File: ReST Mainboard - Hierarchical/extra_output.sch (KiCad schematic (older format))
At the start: 16 parts, among them P28 CONN_02X02, P32 CONN_02X02, P33 CONN_02X02, P34 CONN_02X02, Q1 TBD, Q2 TBD, Q3 TBD, Q4 TBD

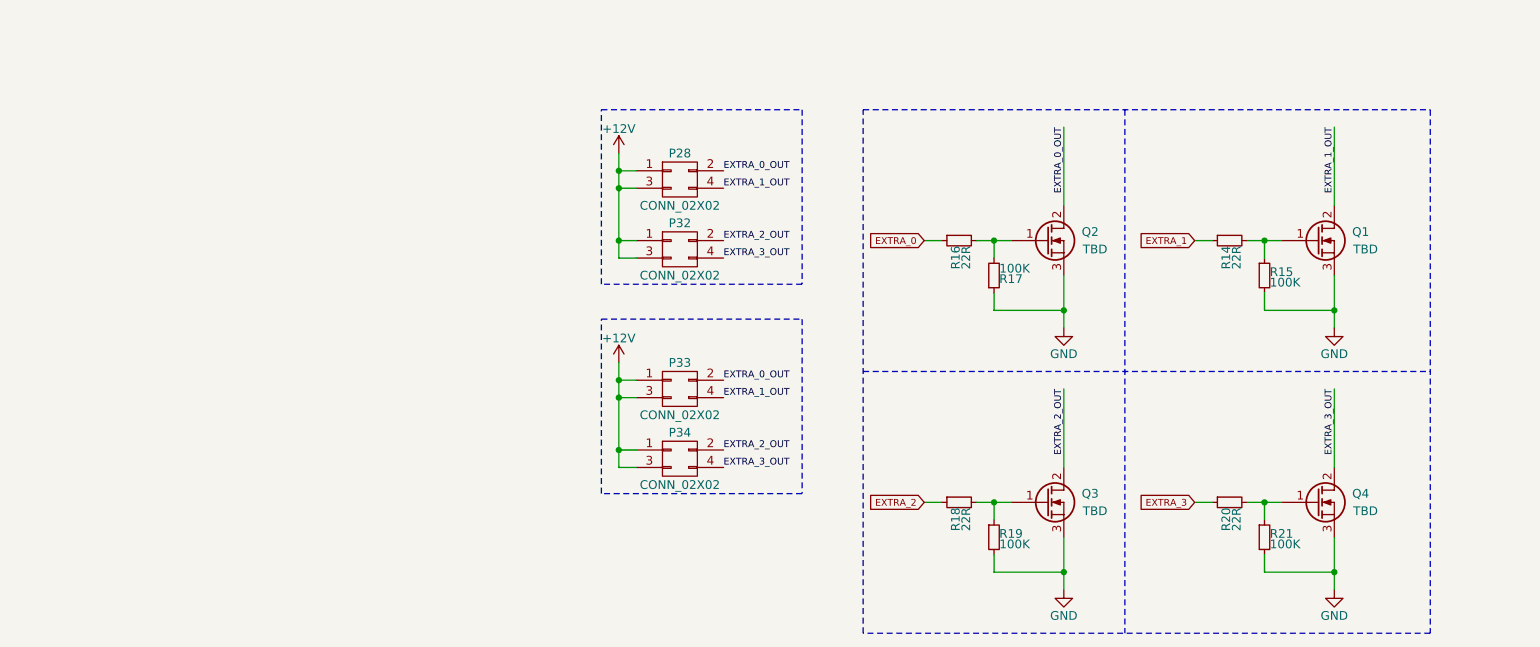
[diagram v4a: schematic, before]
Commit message: changed extra output schematic
added 3->5V level transtor. changed footprints. changed resistor
footprints.
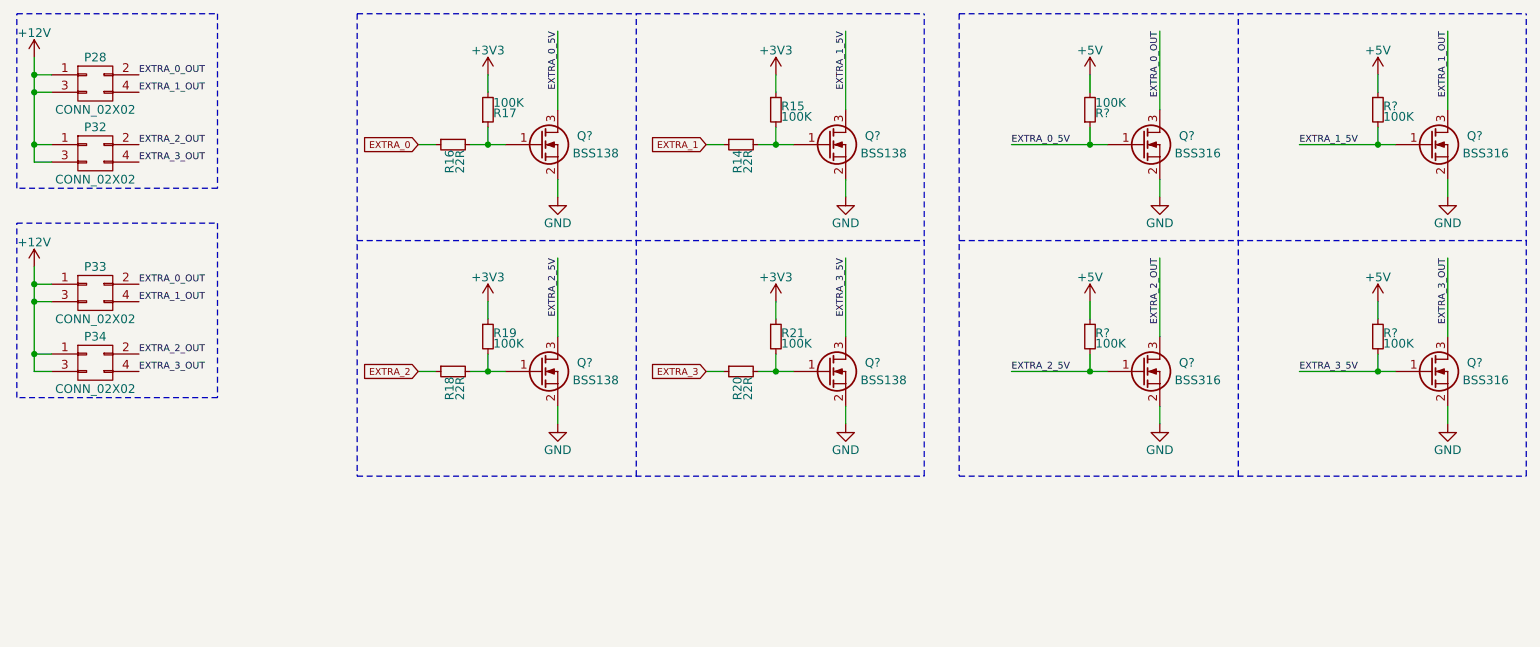
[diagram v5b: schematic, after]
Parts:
- removed Q1, Q2, Q3, Q4: TBD, TO_SOT_Packages_SMD:SOT-23, symbol Q_NMOS_GDS
- added Q? (x4): BSS316, TO_SOT_Packages_SMD:SOT-23, symbol Q_NMOS_GSD
- added Q? (x4): BSS138, TO_SOT_Packages_SMD:SOT-23, symbol Q_NMOS_GSD
- added R? (x4): 100K, Resistors_SMD:R_0805, symbol R_Small
- R14, R15, R16, R17, R18, R19, R20, R21: footprint Resistors_SMD:R_0603_HandSoldering -> Resistors_SMD:R_0805
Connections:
- net EXTRA_0_OUT: now also Q?.3 (D)
- net EXTRA_1_OUT: now also Q?.3 (D)
- net EXTRA_2_OUT: now also Q?.3 (D)
- net EXTRA_3_OUT: now also Q?.3 (D)
- net GND: now also Q?.2 (S), Q?.2 (S), Q?.2 (S), Q?.2 (S), Q?.2 (S), Q?.2 (S), Q?.2 (S), Q?.2 (S); no longer R15.2, R17.1, R19.2, R21.2
- net at R16.2: now also R17.1, Q?.1 (G); no longer R17.2
- net at R14.2: now also R15.2, Q?.1 (G); no longer R15.1
- net at R18.2: now also R19.2, Q?.1 (G); no longer R19.1
- net at R20.2: now also R21.2, Q?.1 (G); no longer R21.1
- new net +3V3: R15.1, R17.2, R19.1, R21.1
- new net +5V: R?.1, R?.1, R?.1, R?.2
- new net EXTRA_0_5V: Q?.1 (G), Q?.3 (D), R?.1
- new net EXTRA_1_5V: Q?.1 (G), Q?.3 (D), R?.2
- new net EXTRA_2_5V: Q?.1 (G), Q?.3 (D), R?.2
- new net EXTRA_3_5V: Q?.1 (G), Q?.3 (D), R?.2
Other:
- moved on the sheet: P28, P32, P33, P34, R14, R15, R16, R17, R18, R19, R20, R21

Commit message: changed 3.3V LDO due to symbol errors
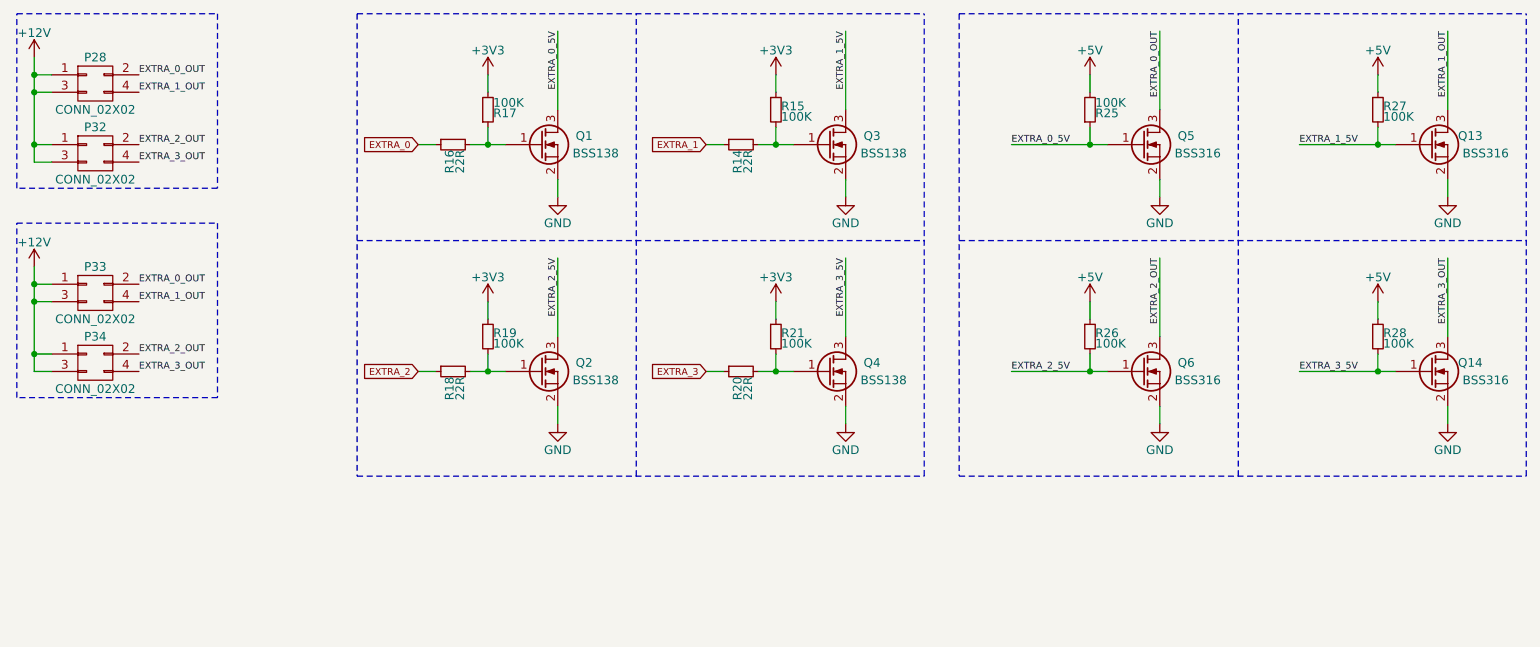
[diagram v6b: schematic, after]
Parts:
- gave numbers to parts that had none: 12
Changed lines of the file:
@@
 $EndComp
 $Comp
-L GND #PWR0118
+L GND #PWR0114
 U 1 1 576EE030
 P 5050 2350
-F 0 "#PWR0118" H 5050 2100 50  0001 C CNN
+F 0 "#PWR0114" H 5050 2100 50  0001 C CNN
 F 1 "GND" H 5050 2200 50  0000 C CNN
 F 2 "" H 5050 2350 50  0000 C CNN
@@
 $EndComp
 $Comp
-L GND #PWR0119
+L GND #PWR0115
 U 1 1 576EE0FE
 P 6700 2350
-F 0 "#PWR0119" H 6700 2100 50  0001 C CNN
+F 0 "#PWR0115" H 6700 2100 50  0001 C CNN
 F 1 "GND" H 6700 2200 50  0000 C CNN
 F 2 "" H 6700 2350 50  0000 C CNN
@@
 $EndComp
 $Comp
-L GND #PWR0120
+L GND #PWR0116
 U 1 1 576EE158
 P 5050 3650
-F 0 "#PWR0120" H 5050 3400 50  0001 C CNN
+F 0 "#PWR0116" H 5050 3400 50  0001 C CNN
 F 1 "GND" H 5050 3500 50  0000 C CNN
 F 2 "" H 5050 3650 50  0000 C CNN
@@
 $EndComp
 $Comp
-L GND #PWR0121
+L GND #PWR0117
 U 1 1 576EE1CA
 P 6700 3650
-F 0 "#PWR0121" H 6700 3400 50  0001 C CNN
+F 0 "#PWR0117" H 6700 3400 50  0001 C CNN
 F 1 "GND" H 6700 3500 50  0000 C CNN
 F 2 "" H 6700 3650 50  0000 C CNN
@@
 $EndComp
 $Comp
-L +12V #PWR0122
+L +12V #PWR0118
 U 1 1 576F0789
 P 2050 1550
-F 0 "#PWR0122" H 2050 1400 50  0001 C CNN
+F 0 "#PWR0118" H 2050 1400 50  0001 C CNN
 F 1 "+12V" H 2050 1690 50  0000 C CNN
 F 2 "" H 2050 1550 50  0000 C CNN
@@
 $EndComp
 $Comp
-L +12V #PWR0123
+L +12V #PWR0119
 U 1 1 576F6790
 P 2050 2750
-F 0 "#PWR0123" H 2050 2600 50  0001 C CNN
+F 0 "#PWR0119" H 2050 2600 50  0001 C CNN
 F 1 "+12V" H 2050 2890 50  0000 C CNN
 F 2 "" H 2050 2750 50  0000 C CNN
@@
 Connection ~ 6300 3350
 $Comp
-L +3V3 #PWR?
+L +3V3 #PWR0120
 U 1 1 57E57454
 P 6300 2950
-F 0 "#PWR?" H 6300 2800 50  0001 C CNN
+F 0 "#PWR0120" H 6300 2800 50  0001 C CNN
 F 1 "+3V3" H 6300 3090 50  0000 C CNN
 F 2 "" H 6300 2950 50  0000 C CNN
@@
 $EndComp
 $Comp
-L +5V #PWR?
+L +5V #PWR0121
 U 1 1 57E574C8
 P 9750 2950
-F 0 "#PWR?" H 9750 2800 50  0001 C CNN
+F 0 "#PWR0121" H 9750 2800 50  0001 C CNN
 F 1 "+5V" H 9750 3090 50  0000 C CNN
 F 2 "" H 9750 2950 50  0000 C CNN
@@
 	6300 1650 6300 1750
 $Comp
-L +3V3 #PWR?
+L +3V3 #PWR0122
 U 1 1 57E58259
 P 4650 2950
-F 0 "#PWR?" H 4650 2800 50  0001 C CNN
+F 0 "#PWR0122" H 4650 2800 50  0001 C CNN
 F 1 "+3V3" H 4650 3090 50  0000 C CNN
 F 2 "" H 4650 2950 50  0000 C CNN
@@
 $EndComp
 $Comp
-L +3V3 #PWR?
+L +3V3 #PWR0123
 U 1 1 57E58294
 P 4650 1650
-F 0 "#PWR?" H 4650 1500 50  0001 C CNN
+F 0 "#PWR0123" H 4650 1500 50  0001 C CNN
 F 1 "+3V3" H 4650 1790 50  0000 C CNN
 F 2 "" H 4650 1650 50  0000 C CNN
@@
 $EndComp
 $Comp
-L +3V3 #PWR?
+L +3V3 #PWR0124
 U 1 1 57E5830F
 P 6300 1650
-F 0 "#PWR?" H 6300 1500 50  0001 C CNN
+F 0 "#PWR0124" H 6300 1500 50  0001 C CNN
 F 1 "+3V3" H 6300 1790 50  0000 C CNN
 F 2 "" H 6300 1650 50  0000 C CNN
@@
 	5500 3950 5500 1300
 $Comp
-L GND #PWR?
+L GND #PWR0125
 U 1 1 57E59C25
 P 8500 2350
-F 0 "#PWR?" H 8500 2100 50  0001 C CNN
+F 0 "#PWR0125" H 8500 2100 50  0001 C CNN
 F 1 "GND" H 8500 2200 50  0000 C CNN
 F 2 "" H 8500 2350 50  0000 C CNN
@@
 	8500 1400 8500 1850
 $Comp
-L GND #PWR?
+L GND #PWR0126
 U 1 1 57E59C3D
 P 10150 2350
-F 0 "#PWR?" H 10150 2100 50  0001 C CNN
+F 0 "#PWR0126" H 10150 2100 50  0001 C CNN
 F 1 "GND" H 10150 2200 50  0000 C CNN
 F 2 "" H 10150 2350 50  0000 C CNN
@@
 	10150 1400 10150 1850
 $Comp
-L GND #PWR?
+L GND #PWR0127
 U 1 1 57E59C55
 P 8500 3650
-F 0 "#PWR?" H 8500 3400 50  0001 C CNN
+F 0 "#PWR0127" H 8500 3400 50  0001 C CNN
 F 1 "GND" H 8500 3500 50  0000 C CNN
 F 2 "" H 8500 3650 50  0000 C CNN
@@
 	8500 2700 8500 3150
 $Comp
-L GND #PWR?
+L GND #PWR0128
 U 1 1 57E59C6D
 P 10150 3650
-F 0 "#PWR?" H 10150 3400 50  0001 C CNN
+F 0 "#PWR0128" H 10150 3400 50  0001 C CNN
 F 1 "GND" H 10150 3500 50  0000 C CNN
 F 2 "" H 10150 3650 50  0000 C CNN
@@
 	10150 2700 10150 3150
 $Comp
-L R_Small R?
+L R_Small R25
 U 1 1 57E59C78
 P 8100 1850
-F 0 "R?" H 8130 1870 50  0000 L CNN
+F 0 "R25" H 8130 1870 50  0000 L CNN
 F 1 "100K" H 8130 1810 50  0000 L CNN
 F 2 "Resistors_SMD:R_0805" H 8100 1850 50  0001 C CNN
@@
 $EndComp
 $Comp
-L R_Small R?
+L R_Small R27
 U 1 1 57E59C7E
 P 9750 1850
-F 0 "R?" H 9780 1870 50  0000 L CNN
+F 0 "R27" H 9780 1870 50  0000 L CNN
 F 1 "100K" H 9780 1810 50  0000 L CNN
 F 2 "Resistors_SMD:R_0805" H 9750 1850 50  0001 C CNN
@@
 $EndComp
 $Comp
-L R_Small R?
+L R_Small R26
 U 1 1 57E59C84
 P 8100 3150
-F 0 "R?" H 8130 3170 50  0000 L CNN
+F 0 "R26" H 8130 3170 50  0000 L CNN
 F 1 "100K" H 8130 3110 50  0000 L CNN
 F 2 "Resistors_SMD:R_0805" H 8100 3150 50  0001 C CNN
@@
 $EndComp
 $Comp
-L R_Small R?
+L R_Small R28
 U 1 1 57E59C8A
 P 9750 3150
-F 0 "R?" H 9780 3170 50  0000 L CNN
+F 0 "R28" H 9780 3170 50  0000 L CNN
 F 1 "100K" H 9780 3110 50  0000 L CNN
 F 2 "Resistors_SMD:R_0805" H 9750 3150 50  0001 C CNN
@@
 EXTRA_0_5V
 $Comp
-L Q_NMOS_GSD Q?
+L Q_NMOS_GSD Q5
 U 1 1 57E5B1A7
 P 8400 2050
-F 0 "Q?" H 8700 2100 50  0000 R CNN
+F 0 "Q5" H 8700 2100 50  0000 R CNN
 F 1 "BSS316" H 8850 2000 50  0000 R CNN
 F 2 "TO_SOT_Packages_SMD:SOT-23" H 8600 2150 50  0001 C CNN
@@
 $EndComp
 $Comp
-L Q_NMOS_GSD Q?
+L Q_NMOS_GSD Q13
 U 1 1 57E5B45C
 P 10050 2050
-F 0 "Q?" H 10350 2100 50  0000 R CNN
+F 0 "Q13" H 10350 2100 50  0000 R CNN
 F 1 "BSS316" H 10500 2000 50  0000 R CNN
 F 2 "TO_SOT_Packages_SMD:SOT-23" H 10250 2150 50  0001 C CNN
@@
 $EndComp
 $Comp
-L Q_NMOS_GSD Q?
+L Q_NMOS_GSD Q14
 U 1 1 57E5B520
 P 10050 3350
-F 0 "Q?" H 10350 3400 50  0000 R CNN
+F 0 "Q14" H 10350 3400 50  0000 R CNN
 F 1 "BSS316" H 10500 3300 50  0000 R CNN
 F 2 "TO_SOT_Packages_SMD:SOT-23" H 10250 3450 50  0001 C CNN
@@
 $EndComp
 $Comp
-L Q_NMOS_GSD Q?
+L Q_NMOS_GSD Q6
 U 1 1 57E5B562
 P 8400 3350
-F 0 "Q?" H 8700 3400 50  0000 R CNN
+F 0 "Q6" H 8700 3400 50  0000 R CNN
 F 1 "BSS316" H 8850 3300 50  0000 R CNN
 F 2 "TO_SOT_Packages_SMD:SOT-23" H 8600 3450 50  0001 C CNN
@@
 $EndComp
 $Comp
-L Q_NMOS_GSD Q?
+L Q_NMOS_GSD Q1
 U 1 1 57E5BA06
 P 4950 2050
-F 0 "Q?" H 5250 2100 50  0000 R CNN
+F 0 "Q1" H 5250 2100 50  0000 R CNN
 F 1 "BSS138" H 5400 2000 50  0000 R CNN
 F 2 "TO_SOT_Packages_SMD:SOT-23" H 5150 2150 50  0001 C CNN
@@
 $EndComp
 $Comp
-L Q_NMOS_GSD Q?
+L Q_NMOS_GSD Q3
 U 1 1 57E5BC8F
 P 6600 2050
-F 0 "Q?" H 6900 2100 50  0000 R CNN
+F 0 "Q3" H 6900 2100 50  0000 R CNN
 F 1 "BSS138" H 7050 2000 50  0000 R CNN
 F 2 "TO_SOT_Packages_SMD:SOT-23" H 6800 2150 50  0001 C CNN
@@
 $EndComp
 $Comp
-L Q_NMOS_GSD Q?
+L Q_NMOS_GSD Q4
 U 1 1 57E5BCCB
 P 6600 3350
-F 0 "Q?" H 6900 3400 50  0000 R CNN
+F 0 "Q4" H 6900 3400 50  0000 R CNN
 F 1 "BSS138" H 7050 3300 50  0000 R CNN
 F 2 "TO_SOT_Packages_SMD:SOT-23" H 6800 3450 50  0001 C CNN
@@
 $EndComp
 $Comp
-L Q_NMOS_GSD Q?
+L Q_NMOS_GSD Q2
 U 1 1 57E5BD0B
 P 4950 3350
-F 0 "Q?" H 5250 3400 50  0000 R CNN
+F 0 "Q2" H 5250 3400 50  0000 R CNN
 F 1 "BSS138" H 5400 3300 50  0000 R CNN
 F 2 "TO_SOT_Packages_SMD:SOT-23" H 5150 3450 50  0001 C CNN
@@
 $EndComp
 $Comp
-L +5V #PWR?
+L +5V #PWR0129
 U 1 1 57E5C6E6
 P 9750 1650
-F 0 "#PWR?" H 9750 1500 50  0001 C CNN
+F 0 "#PWR0129" H 9750 1500 50  0001 C CNN
 F 1 "+5V" H 9750 1790 50  0000 C CNN
 F 2 "" H 9750 1650 50  0000 C CNN
@@
 $EndComp
 $Comp
-L +5V #PWR?
+L +5V #PWR0130
 U 1 1 57E5C739
 P 8100 1650
-F 0 "#PWR?" H 8100 1500 50  0001 C CNN
+F 0 "#PWR0130" H 8100 1500 50  0001 C CNN
 F 1 "+5V" H 8100 1790 50  0000 C CNN
 F 2 "" H 8100 1650 50  0000 C CNN
@@
 $EndComp
 $Comp
-L +5V #PWR?
+L +5V #PWR0131
 U 1 1 57E5C78C
 P 8100 2950
-F 0 "#PWR?" H 8100 2800 50  0001 C CNN
+F 0 "#PWR0131" H 8100 2800 50  0001 C CNN
 F 1 "+5V" H 8100 3090 50  0000 C CNN
 F 2 "" H 8100 2950 50  0000 C CNN
